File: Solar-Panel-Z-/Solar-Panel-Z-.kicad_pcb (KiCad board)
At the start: 6 copper layers, 113.8 x 48.5 mm, 86 parts, among them J1 FFC2B28-10-G, J1 TODO, J2 U.FL-R-SMT-1, Q1 IRLML2803, U1 BQ25570RGRR, U2 TSL2561, U3 NDS8434, U4 ATB2012-50011-T000

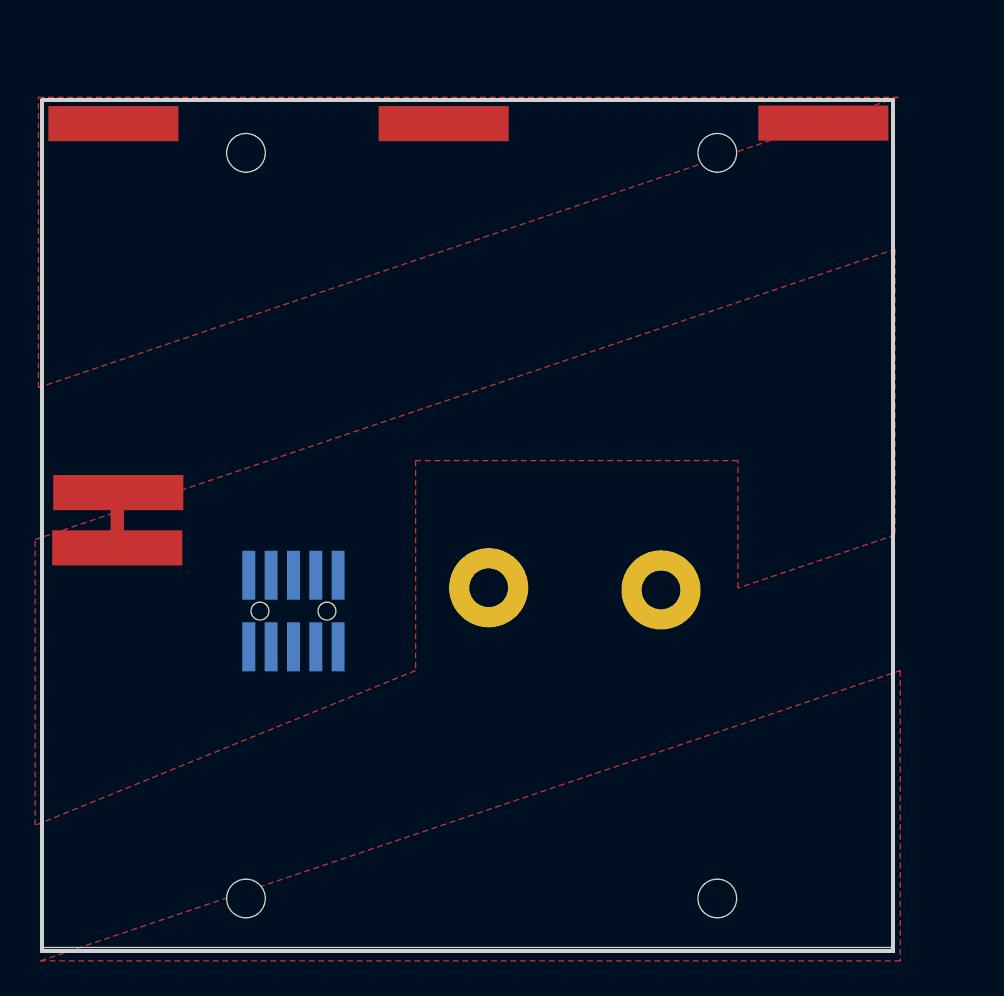
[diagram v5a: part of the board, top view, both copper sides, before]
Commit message: Copied more of previous board
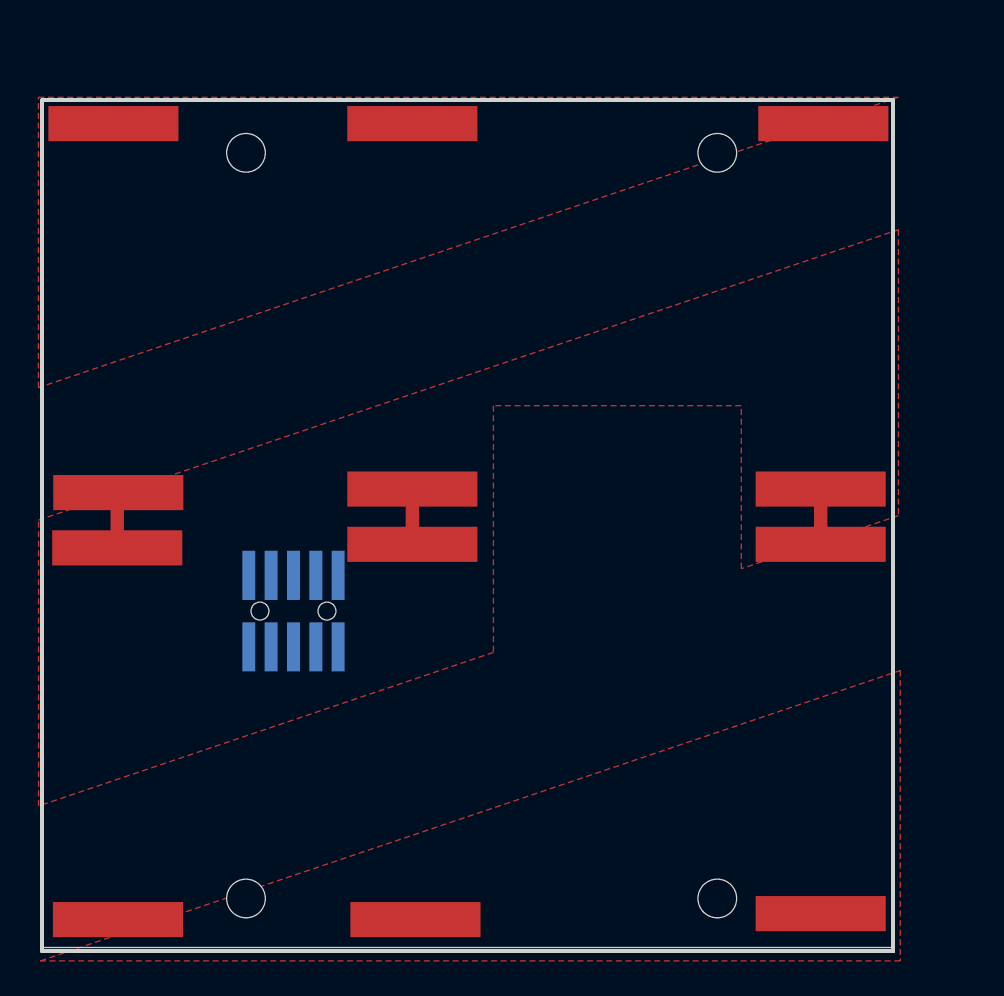
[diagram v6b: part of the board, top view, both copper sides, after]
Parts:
- removed the ? at (51.8, 72.1)
- removed the ? at (42.0, 72.0)
- added ?: , , F.Cu at (37.7, 69.5)
- added ?: , , F.Cu at (60.5, 90.5)
- added ?: , , F.Cu at (20.9, 90.9)
- added ?: , , F.Cu at (37.7, 66.4)
- added ?: , , F.Cu at (60.9, 69.5)
- added ?: , , F.Cu at (37.8, 90.9)
- added ?: , , F.Cu at (60.9, 66.4)
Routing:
- net (no net): track 440.2 -> 446.5 mm
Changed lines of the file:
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@@
       (effects (font (size 1.27 1.27) (thickness 0.15)))
     )
-    (pad "1" smd rect (at 0 0 270) (size 2 7.4) (layers "F.Cu" "F.Paste" "F.Mask")
+    (pad "1" smd rect (at -1.780006 0 270) (size 2 7.4) (layers "F.Cu" "F.Paste" "F.Mask")
       (pinfunction "V+") (pintype "bidirectional"))
   )
@@
       (pinfunction "V-") (pintype "bidirectional"))
   )
+  (footprint "" (layer "F.Cu")
+    (at 20.92 90.87)
+    (fp_text reference "" (at 0 0) (layer "F.SilkS")
+      (effects (font (size 1.27 1.27) (thickness 0.15)))
+    )
+    (fp_text value "" (at 0 0) (layer "F.SilkS")
+      (effects (font (size 1.27 1.27) (thickness 0.15)))
+    )
+    (pad "2" smd rect (at 0 0 270) (size 2 7.4) (layers "F.Cu" "F.Paste" "F.Mask")
+      (pinfunction "V-") (pintype "bidirectional"))
+  )
+  (footprint "" (layer "F.Cu")
+    (at 37.659996 66.388996)
+    (fp_text reference "" (at 0 0) (layer "F.SilkS")
+      (effects (font (size 1.27 1.27) (thickness 0.15)))
+    )
+    (fp_text value "" (at 0 0) (layer "F.SilkS")
+      (effects (font (size 1.27 1.27) (thickness 0.15)))
+    )
+    (pad "2" smd rect (at -0.000004 -0.000009 270) (size 2 7.4) (layers "F.Cu" "F.Paste" "F.Mask")
+      (pinfunction "V-") (pintype "bidirectional"))
+  )
+  (footprint "" (layer "F.Cu")
+    (at 60.87999 69.531001)
+    (fp_text reference "" (at 0 0) (layer "F.SilkS")
+      (effects (font (size 1.27 1.27) (thickness 0.15)))
+    )
+    (fp_text value "" (at 0 0) (layer "F.SilkS")
+      (effects (font (size 1.27 1.27) (thickness 0.15)))
+    )
+    (pad "1" smd rect (at 0 0 270) (size 2 7.4) (layers "F.Cu" "F.Paste" "F.Mask")
+      (pinfunction "V+") (pintype "bidirectional"))
+  )
   (footprint "Fiducial:Fiducial_0.75mm_Mask1.5mm" (layer "F.Cu")
     (at 120.4785 45.941102 -90)
@@
   )
   (footprint "" (layer "F.Cu")
-    (at 51.8 72.125)
+    (at 37.836099 90.869992)
     (fp_text reference "" (at 0 0) (layer "F.SilkS")
       (effects (font (size 1.27 1.27) (thickness 0.15)))
@@
       (effects (font (size 1.27 1.27) (thickness 0.15)))
     )
-    (pad "1" thru_hole circle (at 0 0 90) (size 4.5 4.5) (drill 2.2) (layers *.Cu *.Mask)
-      (net 2 "Net-(H5-Pad1)") (pinfunction "1") (pintype "input"))
+    (pad "2" smd rect (at 0 0 270) (size 2 7.4) (layers "F.Cu" "F.Paste" "F.Mask")
+      (pinfunction "V-") (pintype "bidirectional"))
+  )
+  (footprint "" (layer "F.Cu")
+    (at 60.87999 66.388996)
+    (fp_text reference "" (at 0 0) (layer "F.SilkS")
+      (effects (font (size 1.27 1.27) (thickness 0.15)))
+    )
+    (fp_text value "" (at 0 0) (layer "F.SilkS")
+      (effects (font (size 1.27 1.27) (thickness 0.15)))
+    )
+    (pad "2" smd rect (at 0 0 270) (size 2 7.4) (layers "F.Cu" "F.Paste" "F.Mask")
+      (pinfunction "V-") (pintype "bidirectional"))
   )
   (footprint "Fiducial:Fiducial_0.75mm_Mask1.5mm" (layer "F.Cu")
@@
   )
   (footprint "" (layer "F.Cu")
-    (at 61.03 45.58)
+    (at 61.030002 45.609993)
     (fp_text reference "" (at 0 0) (layer "F.SilkS")
       (effects (font (size 1.27 1.27) (thickness 0.15)))
@@
   )
   (footprint "" (layer "F.Cu")
+    (at 37.66 69.530994)
+    (fp_text reference "" (at 0 0) (layer "F.SilkS")
+      (effects (font (size 1.27 1.27) (thickness 0.15)))
+    )
+    (fp_text value "" (at 0 0) (layer "F.SilkS")
+      (effects (font (size 1.27 1.27) (thickness 0.15)))
+    )
+    (pad "1" smd rect (at -0.000004 0.000007 270) (size 2 7.4) (layers "F.Cu" "F.Paste" "F.Mask")
+      (pinfunction "V+") (pintype "bidirectional"))
+  )
+  (footprint "" (layer "F.Cu")
     (at 20.879999 69.732398)
     (fp_text reference "" (at 0 0) (layer "F.SilkS")
@@
     (fp_line (start 17 0) (end 19 0) (layer "F.SilkS") (width 0.12))
     (fp_line (start -1 -4) (end 22 -4) (layer "F.SilkS") (width 0.12))
-    (pad "1" smd rect (at 0 0 270) (size 2 7.4) (layers "F.Cu" "F.Paste" "F.Mask")
+    (pad "1" smd rect (at -0.000003 -0.00001 270) (size 2 7.4) (layers "F.Cu" "F.Paste" "F.Mask")
       (pinfunction "V+") (pintype "bidirectional"))
     (pad "2" smd rect (at 21 0 270) (size 2 7.4) (layers "F.Cu" "F.Paste" "F.Mask")
@@
   )
   (footprint "" (layer "F.Cu")
-    (at 42 72)
+    (at 60.470009 90.53101)
     (fp_text reference "" (at 0 0) (layer "F.SilkS")
       (effects (font (size 1.27 1.27) (thickness 0.15)))
@@
       (effects (font (size 1.27 1.27) (thickness 0.15)))
     )
-    (pad "1" thru_hole circle (at 0 0 270) (size 4.5 4.5) (drill 2.2) (layers *.Cu *.Mask)
-      (net 3 "Net-(H6-Pad1)") (pinfunction "1") (pintype "input"))
+    (pad "2" smd rect (at 0.409987 -0.000001 270) (size 2 7.4) (layers "F.Cu" "F.Paste" "F.Mask")
+      (pinfunction "V-") (pintype "bidirectional"))
   )
   (footprint "Diode_SMD:D_SMA" (layer "F.Cu")
@@
   (gr_circle (center 97.034 49.316212) (end 97.034 51.316212) (layer "F.SilkS") (width 0.05) (fill none))
   (gr_rect (start 114.5095 62.197102) (end 107.9055 74.516102) (layer "F.Mask") (width 0) (fill solid))
-  (gr_rect (start 46.619 64.8405) (end 38 80) (layer "F.Mask") (width 0) (fill solid))
-  (gr_rect (start 56 64.8405) (end 47 80) (layer "F.Mask") (width 0) (fill solid))
   (gr_rect (start 121.4945 62.197102) (end 114.8905 74.516102) (layer "F.Mask") (width 0) (fill solid))
+  (gr_rect (start 49.204 61.9955) (end 42.6 76.6445) (layer "F.Mask") (width 0) (fill solid))
+  (gr_rect (start 56.104 61.9655) (end 49.5 76.6745) (layer "F.Mask") (width 0) (fill solid))
   (gr_line (start 82.043 92.611212) (end 82.043 44.211212) (layer "Edge.Cuts") (width 0.2))
   (gr_line (start 16.6 92.669716) (end 64.999997 92.669716) (layer "Edge.Cuts") (width 0.2))
@@
   (segment (start 86.468201 66.854613) (end 86.468201 69.996612) (width 0.762) (layer "F.Cu") (net 0))
   (segment (start 109.4447 79.403102) (end 109.4447 79.191902) (width 0.508) (layer "F.Cu") (net 0))
+  (segment (start 60.88 66.169) (end 60.88 69.310999) (width 0.762) (layer "F.Cu") (net 0))
   (segment (start 103.3843 66.854615) (end 103.3843 69.996604) (width 0.762) (layer "F.Cu") (net 0))
   (segment (start 20.88 66.348001) (end 20.88 69.49) (width 0.762) (layer "F.Cu") (net 0))
   (segment (start 108.6675 80.180302) (end 109.4447 79.403102) (width 0.508) (layer "F.Cu") (net 0))
+  (segment (start 37.66 66.389005) (end 37.66 69.530994) (width 0.762) (layer "F.Cu") (net 0))
   (segment (start 126.018204 66.854613) (end 126.018204 69.996612) (width 0.762) (layer "F.Cu") (net 0))
   (via (at 110.9981 54.196102) (size 0.6) (drill 0.3) (layers "F.Cu" "B.Cu") (net 0))
@@
     )
   )
-  (zone (net 0) (net_name "") (layer "F.Cu") (hatch edge 0.508)
-    (connect_pads (clearance 0.127))
-    (min_thickness 0.254) (filled_areas_thickness no)
-    (fill (thermal_gap 0.508) (thermal_bridge_width 0.508))
-    (polygon
-      (pts
-        (xy 56.173453 72.020418)
-        (xy 56.173453 64.77)
-        (xy 37.846 64.77)
-        (xy 37.846 76.708)
-        (xy 16.212953 85.513574)
-        (xy 16.212953 69.257574)
-        (xy 65.107953 52.747574)
-        (xy 65.107953 69.003574)
-      )
-    )
-  )
   (zone (net 2) (net_name "Net-(H5-Pad1)") (layer "F.Cu") (hatch edge 0.508)
     (connect_pads yes (clearance 0.127))
@@
       )
     )
+  )
+  (zone (net 0) (net_name "") (layer "F.Cu") (hatch edge 0.508)
+    (connect_pads (clearance 0.127))
+    (min_thickness 0.254) (filled_areas_thickness no)
+    (fill (thermal_gap 0.508) (thermal_bridge_width 0.508))
+    (polygon
+      (pts
+        (xy 56.3655 70.916134)
+        (xy 56.3655 61.64918)
+        (xy 42.2685 61.64918)
+        (xy 42.2685 75.67616)
+        (xy 16.405 84.40929)
+        (xy 16.405 68.15329)
+        (xy 65.3 51.64329)
+        (xy 65.3 67.89929)
+      )
+    )

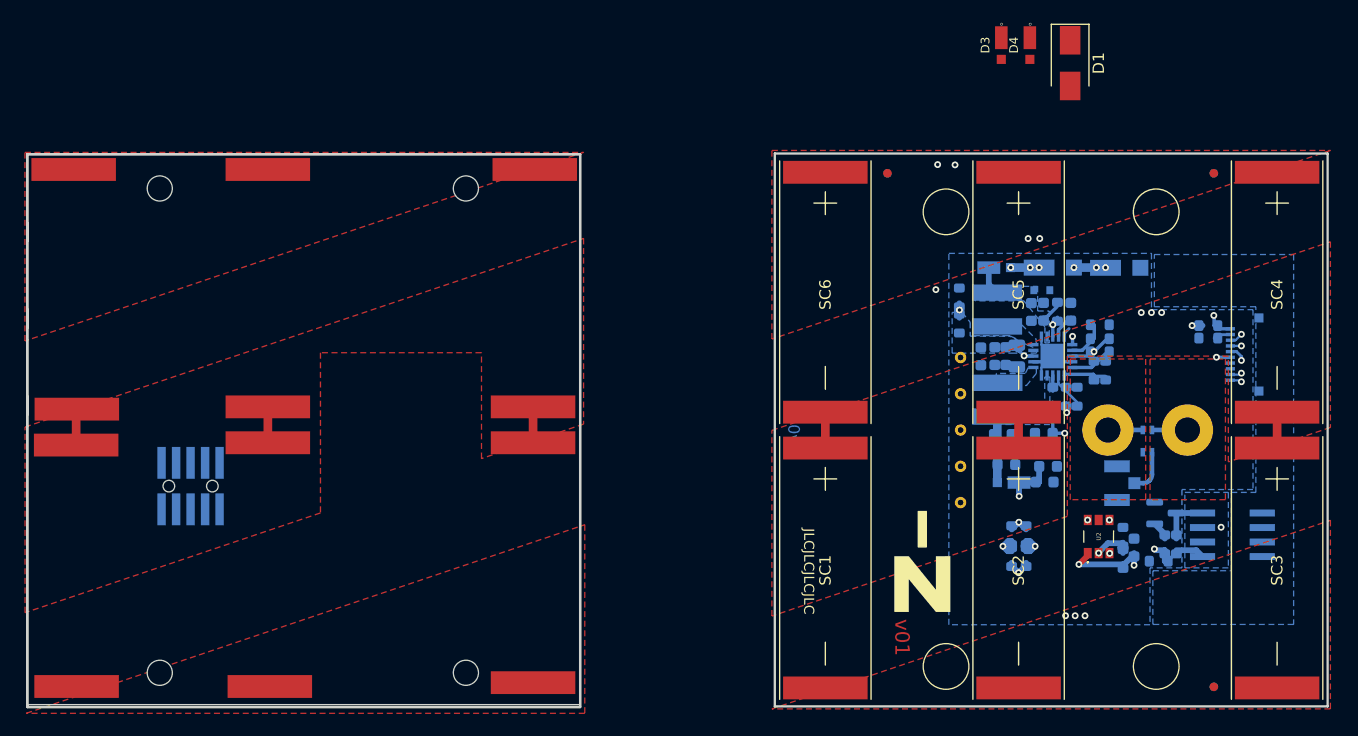
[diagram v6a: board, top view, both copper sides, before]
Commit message: Finish 6 Layer panel versions
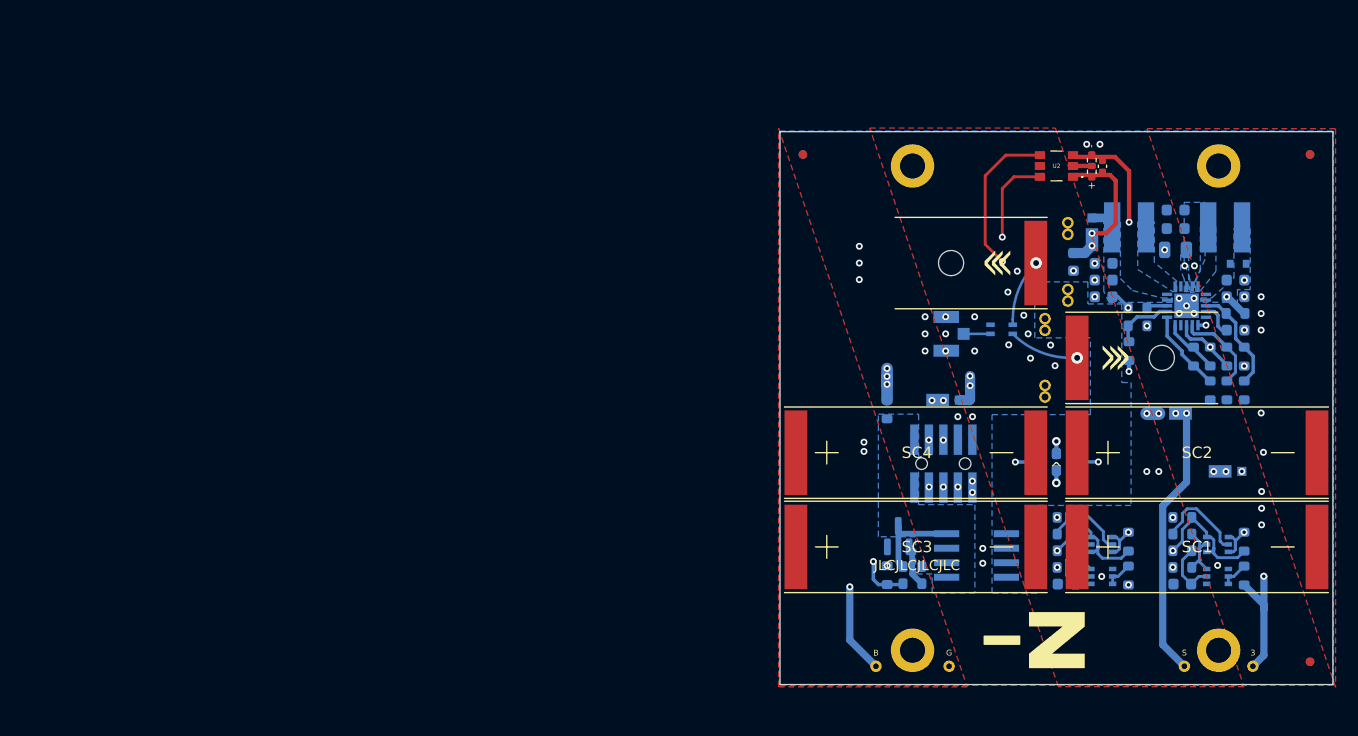
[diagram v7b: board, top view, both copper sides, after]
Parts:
- removed ? (x12): , 
- removed the C11 at (100.1, 62.0)
- removed the C11 at (105.7, 73.0)
- removed C14: 100uF, Capacitor_SMD:C_0603_1608Metric
- removed the D1 at (107.9, 36.3)
- removed the D1 at (105.4, 56.2)
- removed the D3 at (101.9, 34.7)
- removed the D3 at (112.2, 54.2)
- removed the D4 at (104.4, 34.7)
- removed the D4 at (106.4, 54.2)
- removed the J1 at (30.9, 73.3)
- removed the J1 at (123.2, 61.8)
- removed the REF** at (120.5, 45.9) (x2)
- removed the REF** at (120.5, 90.9) (x2)
- removed the REF** at (91.9, 45.9) (x2)
- removed the Ref** at (87.6, 60.0)
- removed SC5, SC6: SolarCell, solarpanels:KXOB25-05X3F
- removed TP5: TP, TestPoint:TestPoint_THTPad_D1.0mm_Drill0.5mm
- added C11: 0.1uF, Capacitor_SMD:C_0603_1608Metric, B.Cu at (108.2, 53.7)
- added C13: 10nF, Capacitor_SMD:C_0603_1608Metric, B.Cu at (107.6, 81.9)
- added D1: SZMM5Z5V1T1G, Diode_SMD:D_SOD-523, B.Cu at (122.6, 53.9)
- added D3: MSS1P4-M3_89A, solarpanels:MICROSMP, B.Cu at (121.7, 72.0)
- added D4: MSS1P4-M3_89A, solarpanels:MICROSMP, B.Cu at (97.0, 65.8)
- added J1: FTS-105-01-L-DV-A, solarpanels:SAMTEC-FTS-105-01-X-DV-A, B.Cu at (96.8, 71.4)
- added JP1: Jumper, solarpanels:Burn-Wire, B.Cu at (107.7, 53.7)
- added JP2: Jumper, solarpanels:Burn-Wire, B.Cu at (105.7, 62.1)
- added Q2: MBT2222ADW1T1, Package_TO_SOT_SMD:SOT-363_SC-70-6, B.Cu at (120.8, 78.4)
- added Q3: BSS138DWQ-7, Package_TO_SOT_SMD:SOT-363_SC-70-6, B.Cu at (110.7, 81.2)
- added Q4: MBT2222ADW1T1, Package_TO_SOT_SMD:SOT-363_SC-70-6, B.Cu at (110.7, 78.4)
- added Q5: IRLML2803, Package_TO_SOT_SMD:SOT-23, B.Cu at (92.8, 77.7)
- added R23: 10K, Resistor_SMD:R_0603_1608Metric, B.Cu at (117.7, 80.4)
- added R24: 10K, Resistor_SMD:R_0603_1608Metric, B.Cu at (117.7, 76.1)
- added R25: 200K, Resistor_SMD:R_0603_1608Metric, B.Cu at (117.7, 79.0)
- added R26: 680, Resistor_SMD:R_0603_1608Metric, B.Cu at (107.6, 77.5)
- added R27: 100K, Resistor_SMD:R_0603_1608Metric, B.Cu at (113.0, 81.2)
- added R28: 10K, Resistor_SMD:R_0603_1608Metric, B.Cu at (107.6, 80.4)
- added R29: 10K, Resistor_SMD:R_0603_1608Metric, B.Cu at (107.6, 76.1)
- added R30: 200K, Resistor_SMD:R_0603_1608Metric, B.Cu at (107.6, 79.0)
- added R31: 10K, Resistor_SMD:R_0603_1608Metric, B.Cu at (91.9, 81.1)
- added R32: 4.7K, Resistor_SMD:R_0603_1608Metric, B.Cu at (94.1, 81.9)
- added R33: 100K, Resistor_SMD:R_0603_1608Metric, B.Cu at (94.1, 80.4)
- added REF**: Fiducial_0.75mm_Mask1.5mm, Fiducial:Fiducial_0.75mm_Mask1.5mm, F.Cu at (128.9, 88.7)
- added REF**: Fiducial_0.75mm_Mask1.5mm, Fiducial:Fiducial_0.75mm_Mask1.5mm, F.Cu at (84.5, 44.3)
- added REF**: Fiducial_0.75mm_Mask1.5mm, Fiducial:Fiducial_0.75mm_Mask1.5mm, F.Cu at (128.9, 44.3)
- added REF**: Fiducial_0.75mm_Mask1.5mm, Fiducial:Fiducial_0.75mm_Mask1.5mm, B.Cu at (128.9, 44.3)
- added REF**: Fiducial_0.75mm_Mask1.5mm, Fiducial:Fiducial_0.75mm_Mask1.5mm, B.Cu at (84.5, 44.3)
- added REF**: Fiducial_0.75mm_Mask1.5mm, Fiducial:Fiducial_0.75mm_Mask1.5mm, B.Cu at (128.9, 88.7)
- added Ref**: Val**, custom-footprints:pycubed_mini_half, B.Cu at (106.7, 44.6)
- C1: footprint Capacitor_SMD:C_0603_1608Metric -> Capacitor_SMD:C_0402_1005Metric; moved to F.Cu
- C12: value 100uF -> 10nF
- H1, H2, H3, H4: footprint MountingHole:MountingHole_2.2mm_M2_DIN965 -> MountingHole:MountingHole_2.2mm_M2_DIN965_Pad; moved to B.Cu
- H5, H6: footprint solarpanels:Antenna Pad -> solarpanels:Antenna Mount
- Q1: value IRLML2803 -> BSS138DWQ-7; footprint Package_TO_SOT_SMD:SOT-23 -> Package_TO_SOT_SMD:SOT-363_SC-70-6
- R1, R2: footprint Resistor_SMD:R_0603_1608Metric -> Resistor_SMD:R_0402_1005Metric; moved to F.Cu
- R14, R15, R19: value 0 -> DNI
- R20: value 10k -> DNI
- R21: value 4.7k -> 680
- R22: value 100k -> 100K
- SC1, SC2, SC3, SC4: value SolarCell -> SolarCell_Small
- U3: value NDS8434 -> ATB2012-50011-T000; footprint solarpanels:NDS8434 -> solarpanels:ATB2012
- U4: value ATB2012-50011-T000 -> NDS8434; footprint solarpanels:ATB2012 -> solarpanels:NDS8434
- moved H4 65.9 mm to (120.9, 87.7), turned to 180 degrees
- moved H1 65.9 mm to (120.9, 45.3), turned to 180 degrees
- moved H2 65.9 mm to (94.1, 45.3), turned to 180 degrees
- moved H3 65.9 mm to (94.1, 87.7), turned to 180 degrees
- moved SC4 48.8 mm to (83.9, 70.4), turned to 0 degrees
- moved SC3 43.0 mm to (83.9, 78.7), turned to 0 degrees
- moved R1 34.0 mm to (109.8, 45.8)
- moved C1 33.5 mm to (110.7, 45.3)
- moved TP1 33.4 mm to (117.9, 89.1), turned to 0 degrees
- moved R2 33.1 mm to (109.8, 44.8)
- moved U2 32.7 mm to (106.7, 45.3), turned to 180 degrees
- moved TP3 31.0 mm to (123.9, 89.1), turned to 0 degrees
- moved R3 29.1 mm to (91.9, 66.6), turned to 90 degrees
- moved U3 27.1 mm to (101.9, 59.6), turned to 0 degrees
- moved R15 26.2 mm to (123.1, 65.0), turned to 90 degrees
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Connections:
- C1 pad 1: (no net) -> GND
- C1 pad 2: (no net) -> +3V3
- C10 pad 1: (no net) -> Net-(C10-Pad1)
- C10 pad 2: (no net) -> GND
- C12 pad 1: (no net) -> Net-(C12-Pad1)
- C12 pad 2: (no net) -> GND
- C2 pad 1: (no net) -> VSOLAR
- C2 pad 2: (no net) -> GND
- C3 pad 1: (no net) -> VSOLAR
- C3 pad 2: (no net) -> GND
- C4 pad 1: (no net) -> Net-(C4-Pad1)
- C4 pad 2: (no net) -> GND
- C5 pad 1: (no net) -> VBAT
- C5 pad 2: (no net) -> GND
- C6 pad 1: (no net) -> VOUT_EN
- C6 pad 2: (no net) -> GND
- C7 pad 1: (no net) -> Net-(C7-Pad1)
- C7 pad 2: (no net) -> GND
- C8 pad 1: (no net) -> Net-(C10-Pad1)
- C8 pad 2: (no net) -> GND
- C9 pad 1: (no net) -> Net-(C7-Pad1)
- C9 pad 2: (no net) -> GND
- D2 pad 1: (no net) -> +3V3
- D2 pad 2: (no net) -> Net-(C10-Pad1)
- D5 pad 1: (no net) -> VSOLAR
- D5 pad 2: (no net) -> /VSOLAR_FULL
- J2 pad 1: (no net) -> GND
- J2 pad 2: (no net) -> GND
- J2 pad 3: (no net) -> Net-(J2-Pad3)
- L1 pad 1: (no net) -> VSOLAR
- L1 pad 2: (no net) -> Net-(L1-Pad2)
- L2 pad 1: (no net) -> Net-(L2-Pad1)
- L2 pad 2: (no net) -> Net-(C10-Pad1)
- Q1 pad 1: (no net) -> GND
- Q1 pad 2: (no net) -> Net-(Q1-Pad2)
- Q1 pad 3: (no net) -> Net-(Q1-Pad2)
- R1 pad 1: (no net) -> Net-(R1-Pad1)
- R1 pad 2: (no net) -> +3V3
- R10 pad 1: (no net) -> Net-(R10-Pad1)
- R10 pad 2: (no net) -> Net-(R10-Pad2)
- R11 pad 1: (no net) -> GND
- R11 pad 2: (no net) -> Net-(R10-Pad1)
- R12 pad 1: (no net) -> COIL_P
- R13 pad 2: (no net) -> COIL_P
- R14 pad 1: (no net) -> Net-(R14-Pad1)
- R14 pad 2: (no net) -> VSOLAR
- R15 pad 1: (no net) -> GND
- R15 pad 2: (no net) -> Net-(R14-Pad1)
- R16 pad 1: (no net) -> Net-(C7-Pad1)
- R16 pad 2: (no net) -> Net-(R14-Pad1)
- R17 pad 1: (no net) -> COIL_N
- R18 pad 2: (no net) -> COIL_N
- R19 pad 1: (no net) -> SCL_LS
- R19 pad 2: (no net) -> SCL
- R2 pad 1: (no net) -> GND
- R2 pad 2: (no net) -> Net-(R1-Pad1)
- R20 pad 1: (no net) -> SDA_LS
- R20 pad 2: (no net) -> SDA
- R21 pad 1: (no net) -> Net-(Q2-Pad2)
- R21 pad 2: (no net) -> Net-(Q1-Pad6)
- R22 pad 1: (no net) -> +3V3
- R22 pad 2: (no net) -> Net-(Q1-Pad2)
- R3 pad 1: (no net) -> BATT_P
- R3 pad 2: (no net) -> VBAT
- R4 pad 1: (no net) -> VBAT_OK
- R4 pad 2: (no net) -> VOUT_EN
- R5 pad 1: (no net) -> Net-(R5-Pad1)
- R5 pad 2: (no net) -> Net-(R10-Pad2)
- R6 pad 1: (no net) -> GND
- R6 pad 2: (no net) -> Net-(R5-Pad1)
- R7 pad 1: (no net) -> Net-(R7-Pad1)
- R7 pad 2: (no net) -> Net-(R10-Pad2)
- R8 pad 1: (no net) -> Net-(R8-Pad1)
- R8 pad 2: (no net) -> Net-(R7-Pad1)
- R9 pad 1: (no net) -> GND
- R9 pad 2: (no net) -> Net-(R8-Pad1)
- SC1 pad 1: (no net) -> Net-(D3-Pad1)
- SC1 pad 2: (no net) -> GND
- SC2 pad 1: (no net) -> Net-(D3-Pad1)
- SC2 pad 2: (no net) -> GND
- SC3 pad 1: (no net) -> /VSOLAR_FULL
- SC3 pad 2: (no net) -> Net-(D3-Pad1)
- SC4 pad 1: (no net) -> /VSOLAR_FULL
- SC4 pad 2: (no net) -> Net-(D3-Pad1)
- TP1 pad 1: (no net) -> VSOLAR
- TP2 pad 1: (no net) -> GND
- TP3 pad 1: (no net) -> +3V3
- TP4 pad 1: (no net) -> VBAT
- U1 pad 1: (no net) -> GND
- U1 pad 10: (no net) -> Net-(R7-Pad1)
- U1 pad 11: (no net) -> Net-(R8-Pad1)
- U1 pad 12: (no net) -> Net-(R10-Pad1)
- U1 pad 13: (no net) -> VBAT_OK
- U1 pad 14: (no net) -> Net-(C10-Pad1)
- U1 pad 15: (no net) -> GND
- U1 pad 16: (no net) -> Net-(L2-Pad1)
- U1 pad 17: (no net) -> GND
- U1 pad 18: (no net) -> VBAT
- U1 pad 19: (no net) -> Net-(C7-Pad1)
- U1 pad 2: (no net) -> VSOLAR
- U1 pad 20: (no net) -> Net-(L1-Pad2)
- U1 pad 21: (no net) -> GND
- U1 pad 3: (no net) -> Net-(R14-Pad1)
- U1 pad 4: (no net) -> Net-(C4-Pad1)
- U1 pad 5: (no net) -> GND
- U1 pad 6: (no net) -> VOUT_EN
- U1 pad 7: (no net) -> Net-(R5-Pad1)
- U1 pad 8: (no net) -> Net-(R10-Pad2)
- U1 pad 9: (no net) -> GND
- U2 pad 1: (no net) -> +3V3
- U2 pad 2: (no net) -> Net-(R1-Pad1)
- U2 pad 3: (no net) -> GND
- U2 pad 4: (no net) -> SCL_LS
- U2 pad 5: (no net) -> unconnected-(U2-Pad5)
- U2 pad 6: (no net) -> SDA_LS
- U3 pad 1: (no net) -> Net-(J2-Pad3)
- U3 pad 2: (no net) -> GND
- U3 pad 3: (no net) -> Net-(H6-Pad1)
- U3 pad 4: (no net) -> Net-(H5-Pad1)
- U4 pad 1: (no net) -> BATT_P
- U4 pad 2: (no net) -> BATT_P
- U4 pad 3: Net-(H6-Pad1) -> BATT_P
- U4 pad 4: Net-(H5-Pad1) -> Net-(Q5-Pad3)
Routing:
- net /coil: track 14800.7 -> 10648.9 mm
- net (no net): track 446.5 -> 0.00 mm, vias 40 -> 0
- net SCL_LS: track 0.00 -> 62.3 mm, vias 0 -> 2
- net SDA_LS: track 0.00 -> 49.8 mm, vias 0 -> 2
- net VSOLAR: track 0.00 -> 43.6 mm, vias 0 -> 4
- net SCL: track 0.00 -> 38.0 mm, vias 0 -> 2
- net /VSOLAR_FULL: track 0.00 -> 31.8 mm, vias 0 -> 6
- net SDA: track 0.00 -> 24.3 mm, vias 0 -> 2
- net +3V3: track 0.00 -> 23.0 mm, vias 0 -> 10
- net BURN1: track 0.00 -> 16.8 mm, vias 0 -> 2
- net COIL_P: track 0.00 -> 15.9 mm, vias 0 -> 2
- net Net-(R10-Pad2): track 0.00 -> 15.3 mm, vias 0 -> 2
- net VBAT: track 0.00 -> 11.3 mm, vias 0 -> 5
- net COIL_N: track 0.00 -> 11.0 mm, vias 0 -> 2
- net Net-(C7-Pad1): track 0.00 -> 10.6 mm, vias 0 -> 2
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- added copper zone on In3.Cu, net +3V3
- added copper zone on B.Cu, net /VBURN
- added copper zone on F.Cu, net /VSOLAR_FULL
- added copper zone on B.Cu, net BATT_P
- added copper zone on B.Cu, net GND
- added copper zone on F.Cu, net GND
- added copper zone on In1.Cu, net GND
- added copper zone on In4.Cu, net GND
- added copper zone on B.Cu, net Net-(C10-Pad1)
- added copper zone on B.Cu, net Net-(C7-Pad1)
- added copper zone on F.Cu, net Net-(D3-Pad1)
- added copper zone on B.Cu, net Net-(L1-Pad2)
- added copper zone on B.Cu, net Net-(L2-Pad1)
- added copper zone on B.Cu, net VBAT
- added copper zone on In2.Cu, net VBAT
- added copper zone on B.Cu, net VSOLAR
- removed copper zone on B.Cu, net (none)
- removed copper zone on F.Cu, net (none)
- removed copper zone on F.Cu, net Net-(H5-Pad1)
- removed copper zone on F.Cu, net Net-(H6-Pad1)
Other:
- board size 113.8 x 48.5 mm -> 48.4 x 48.4 mm
- board text added: "1.BATT_P 3.SCL 5.COIL_N 7.GND 9.GND"
- board text added: "2.BATT_P 4.SDA 6.COIL_P 8.BURN1 10.3V3"
- board text added: "3"
- board text added: "B"
- board text added: "G"
- board text added: "Rev B2/01"
- board text added: "S"
- board text added: "VBAT"
- board text added: "^"
- board text added: "⊗"
- board text added: "⊙"
- board text removed: "1"
- board text removed: "BATT_P"
- board text removed: "BURN1"
- board text removed: "Cable Pinout 1.BATT_P 2.BATT_N 3.SDA 4.SCL 5.BURN 6.3V3 7.GND 8.GND 9.COIL_N 10.COIL_P"
- board text removed: "v01"
